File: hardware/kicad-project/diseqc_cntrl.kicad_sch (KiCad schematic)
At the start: 27 parts, among them IC1 TPS560200DBVR, J1 Barrel Jack

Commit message: Removed hand solder pads
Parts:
- C1, C2, C3, C4: footprint Capacitor_SMD:C_0603_1608Metric_Pad1.08x0.95mm_HandSolder -> Capacitor_SMD:C_0603_1608Metric
- FB2: footprint Inductor_SMD:L_0603_1608Metric_Pad1.05x0.95mm_HandSolder -> Inductor_SMD:L_0603_1608Metric
- R1, R2, R3, R4, R5: footprint Resistor_SMD:R_0603_1608Metric_Pad0.98x0.95mm_HandSolder -> Resistor_SMD:R_0603_1608Metric
- TP1, TP2, TP26, TP27, TP3, TP5: now left out of the parts list
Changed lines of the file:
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@@
 			)
 		)
-		(property "Footprint" "Resistor_SMD:R_0603_1608Metric_Pad0.98x0.95mm_HandSolder"
+		(property "Footprint" "Resistor_SMD:R_0603_1608Metric"
 			(at 94.742 116.84 90)
 			(hide yes)
@@
 			)
 		)
-		(property "Footprint" "Capacitor_SMD:C_0603_1608Metric_Pad1.08x0.95mm_HandSolder"
+		(property "Footprint" "Capacitor_SMD:C_0603_1608Metric"
 			(at 154.94 38.4048 0)
 			(hide yes)
@@
 			)
 		)
-		(property "Footprint" "Resistor_SMD:R_0603_1608Metric_Pad0.98x0.95mm_HandSolder"
+		(property "Footprint" "Resistor_SMD:R_0603_1608Metric"
 			(at 167.132 57.15 90)
 			(hide yes)
@@
 		(body_style 1)
 		(exclude_from_sim no)
-		(in_bom yes)
+		(in_bom no)
 		(on_board yes)
 		(in_pos_files yes)
@@
 		(body_style 1)
 		(exclude_from_sim no)
-		(in_bom yes)
+		(in_bom no)
 		(on_board yes)
 		(in_pos_files yes)
@@
 		(body_style 1)
 		(exclude_from_sim no)
-		(in_bom yes)
+		(in_bom no)
 		(on_board yes)
 		(in_pos_files yes)
@@
 		(body_style 1)
 		(exclude_from_sim no)
-		(in_bom yes)
+		(in_bom no)
 		(on_board yes)
 		(in_pos_files yes)
@@
 			)
 		)
-		(property "Footprint" "Resistor_SMD:R_0603_1608Metric_Pad0.98x0.95mm_HandSolder"
+		(property "Footprint" "Resistor_SMD:R_0603_1608Metric"
 			(at 167.132 46.99 90)
 			(hide yes)
@@
 			)
 		)
-		(property "Footprint" "Capacitor_SMD:C_0603_1608Metric_Pad1.08x0.95mm_HandSolder"
+		(property "Footprint" "Capacitor_SMD:C_0603_1608Metric"
 			(at 79.7052 120.65 0)
 			(hide yes)
@@
 		(body_style 1)
 		(exclude_from_sim no)
-		(in_bom yes)
+		(in_bom no)
 		(on_board yes)
 		(in_pos_files yes)
@@
 			)
 		)
-		(property "Footprint" "Resistor_SMD:R_0603_1608Metric_Pad0.98x0.95mm_HandSolder"
+		(property "Footprint" "Resistor_SMD:R_0603_1608Metric"
 			(at 94.742 129.54 90)
 			(hide yes)
@@
 			)
 		)
-		(property "Footprint" "Inductor_SMD:L_0603_1608Metric_Pad1.05x0.95mm_HandSolder"
+		(property "Footprint" "Inductor_SMD:L_0603_1608Metric"
 			(at 132.08 145.288 90)
 			(hide yes)
@@
 		(body_style 1)
 		(exclude_from_sim no)
-		(in_bom yes)
+		(in_bom no)
 		(on_board yes)
 		(in_pos_files yes)
@@
 			)
 		)
-		(property "Footprint" "Resistor_SMD:R_0603_1608Metric_Pad0.98x0.95mm_HandSolder"
+		(property "Footprint" "Resistor_SMD:R_0603_1608Metric"
 			(at 29.21 114.808 90)
 			(hide yes)
@@
 			)
 		)
-		(property "Footprint" "Capacitor_SMD:C_0603_1608Metric_Pad1.08x0.95mm_HandSolder"
+		(property "Footprint" "Capacitor_SMD:C_0603_1608Metric"
 			(at 105.1052 50.8 0)
 			(hide yes)
@@
 			)
 		)
-		(property "Footprint" "Capacitor_SMD:C_0603_1608Metric_Pad1.08x0.95mm_HandSolder"
+		(property "Footprint" "Capacitor_SMD:C_0603_1608Metric"
 			(at 87.3252 120.65 0)
 			(hide yes)

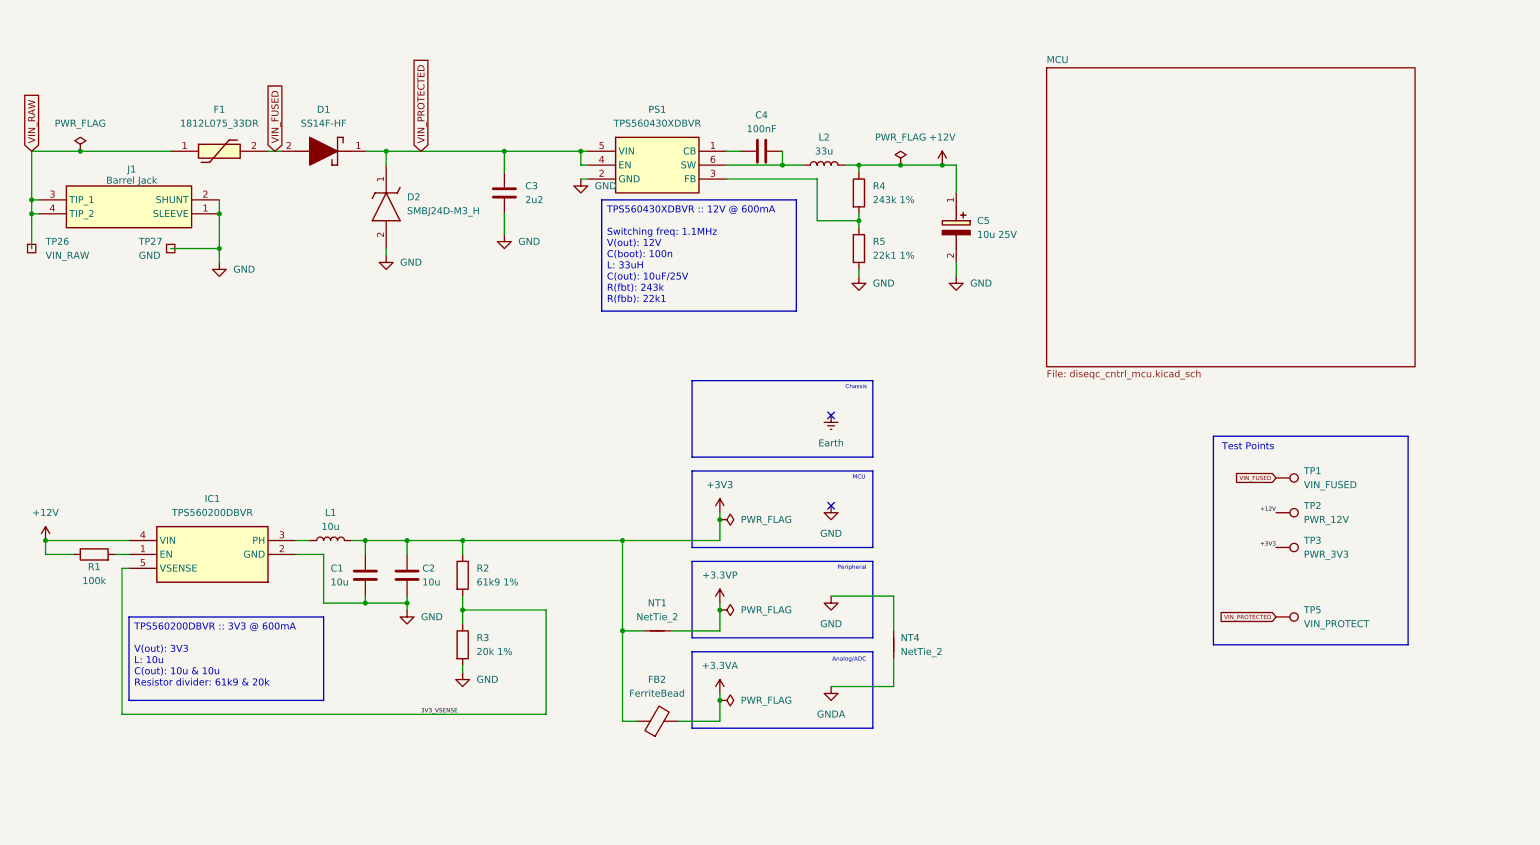
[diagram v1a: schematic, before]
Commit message: Update power supply ICs
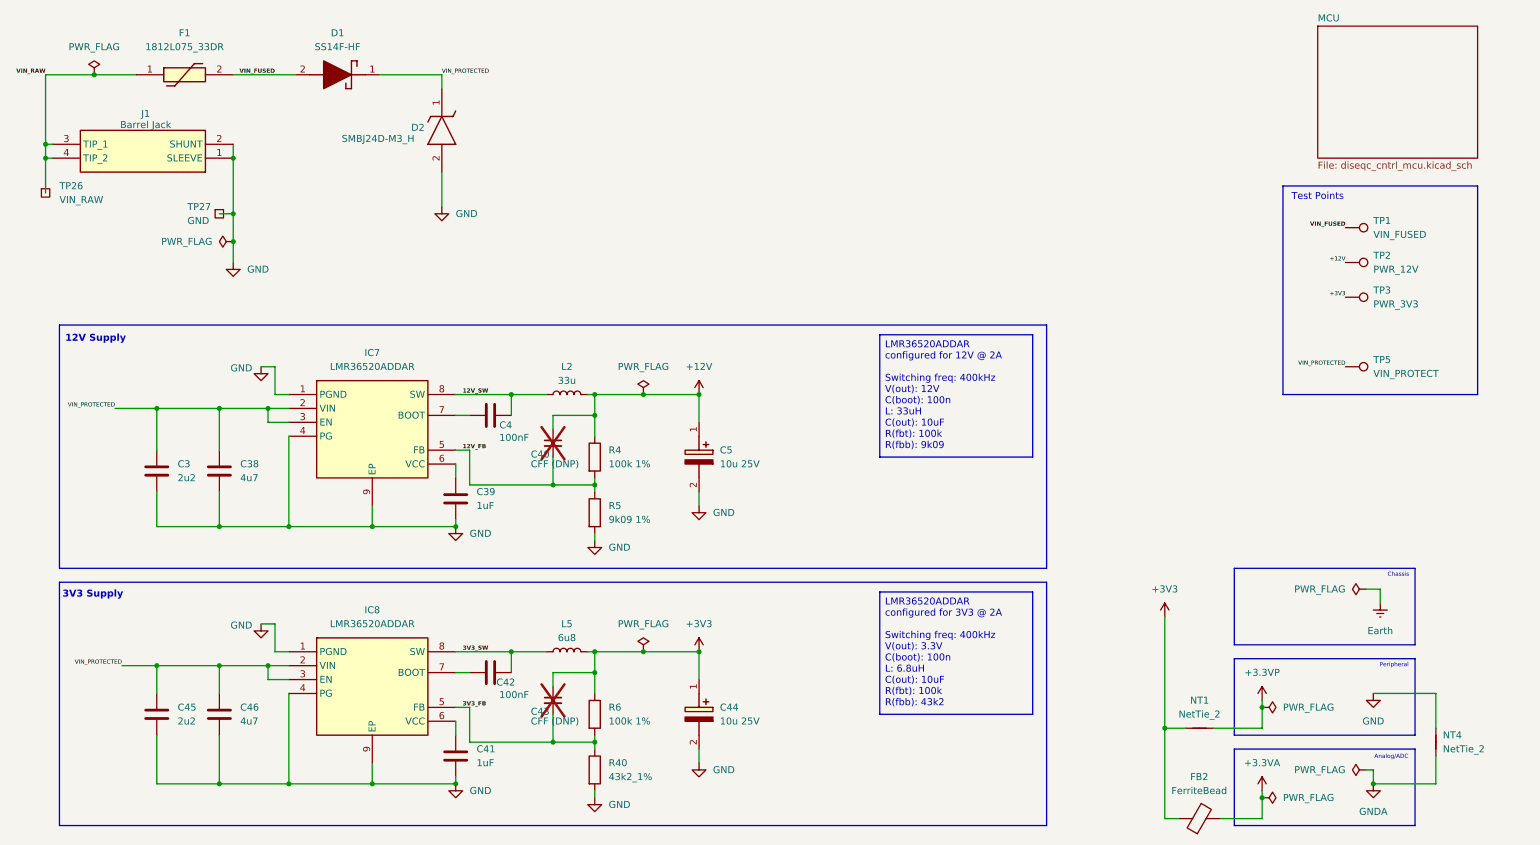
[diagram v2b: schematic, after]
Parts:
- removed C1: 10u, Capacitor_SMD:C_0603_1608Metric, symbol #InvenTree:C_10u_0603
- removed C2: 10u, Capacitor_SMD:C_0603_1608Metric, symbol diseqc_cntrl:C
- removed IC1: TPS560200DBVR, diseqc_cntrl:SOT95P280X145-5N, symbol diseqc_cntrl:TPS560200DBVR
- removed L1: 10u, Inductor_SMD:L_0603_1608Metric_Pad1.05x0.95mm_HandSolder, symbol diseqc_cntrl:L
- removed PS1: TPS560430XDBVR, diseqc_cntrl:SOT95P280X145-6N, symbol tps5604:TPS560430XDBVR
- removed R1: 100k, Resistor_SMD:R_0603_1608Metric, symbol diseqc_cntrl:R
- removed R2: 61k9 1%, Resistor_SMD:R_0603_1608Metric, symbol #InvenTree:R_61k9_0603_1%
- removed R3: 20k 1%, Resistor_SMD:R_0603_1608Metric, symbol #InvenTree:R_20k_0603_1%
- removed R4: 243k 1%, Resistor_SMD:R_0603_1608Metric, symbol diseqc_cntrl:R
- removed R5: 22k1 1%, Resistor_SMD:R_0603_1608Metric, symbol diseqc_cntrl:R
- added C38, C46: 4u7, Capacitor_SMD:C_0603_1608Metric, symbol #InvenTree:C_4u7_0603
- added C39, C41: 1uF, Capacitor_SMD:C_0603_1608Metric, symbol #InvenTree:C_1u_0603
- added C40, C43: CFF (DNP), symbol diseqc_cntrl:C_Small
- added C42: 100nF, Capacitor_SMD:C_0603_1608Metric, symbol diseqc_cntrl:C
- added C44: 10u 25V, diseqc_cntrl:CAPAE400X550N, symbol diseqc_cntrl:865080440002
- added C45: 2u2, Capacitor_SMD:C_0603_1608Metric, symbol diseqc_cntrl:C
- added IC7, IC8: LMR36520ADDAR, ebnx_footprints:SOIC127P600X170-9N, symbol ebnx_symbols:LMR36520ADDAR
- added L5: 6u8, Inductor_SMD:L_0805_2012Metric, symbol #InvenTree:L_6u8_0805
- added R4, R6: 100k 1%, Resistor_SMD:R_0603_1608Metric, symbol #InvenTree:R_100k_0603_1%
- added R40: 43k2_1%, Resistor_SMD:R_0603_1608Metric, symbol #InvenTree:R_43k2_0603_1%
- added R5: 9k09 1%, Resistor_SMD:R_0603_1608Metric, symbol #InvenTree:R_9k09_0603_1%
- L2: footprint diseqc_cntrl:INDPM3030X150N -> ebnx_footprints:INDPM3030X150N
- TP3: now in the parts list
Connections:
- net +12V: now also C40.1, R4.1
- net +3V3: now also C43.1, C44.1 (+), L5.2, R6.1
- net GND: now also C38.2, C39.2, C41.2, C44.2 (-), C45.2, C46.2, IC7.1 (PGND), IC7.4 (PG), IC7.9 (EP), IC8.1 (PGND), IC8.4 (PG), IC8.9 (EP), R40.2, R5.2
- net VIN_PROTECTED: now also C38.1, C45.1, C46.1, IC7.2 (VIN), IC7.3 (EN), IC8.2 (VIN), IC8.3 (EN)
- net at C4.1: now also IC7.7 (BOOT)
- net 12V_SW: now reaches C4.2, L2.1
- net 12V_SW: now also IC7.8 (SW)
- new net: C41.1, IC8.6 (VCC)
- new net: C39.1, IC7.6 (VCC)
- new net: C42.1, IC8.7 (BOOT)
- new net 12V_FB: C40.2, IC7.5 (FB), R4.2, R5.1
- new net 3V3_FB: C43.2, IC8.5 (FB), R40.1, R6.2
- new net 3V3_SW: C42.2, IC8.8 (SW), L5.1
- no-connect marks 2 -> 0
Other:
- note added: "12V Supply"
- note added: "3V3 Supply"
- note removed: "MCU"
- moved on the sheet: D1, D2, F1, FB2, J1, NT1, NT4, TP1, TP2, TP26, TP27, TP3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

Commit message: Renumbered/annotated
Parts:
- renumbered C3 to C1, C43 to C10, C5 to C11, C44 to C12, C45 to C2, C38 to C3, C46 to C4, C39 to C5, C41 to C6, C4 to C7, C42 to C8, C40 to C9, FB2 to FB1, IC7 to IC1, IC8 to IC2, L2 to L1, L5 to L2, NT4 to NT2, R4 to R1, R5 to R2, R6 to R3, R40 to R4, TP26 to TP1, TP27 to TP2, TP1 to TP3, TP2 to TP4, TP3 to TP5, TP5 to TP6

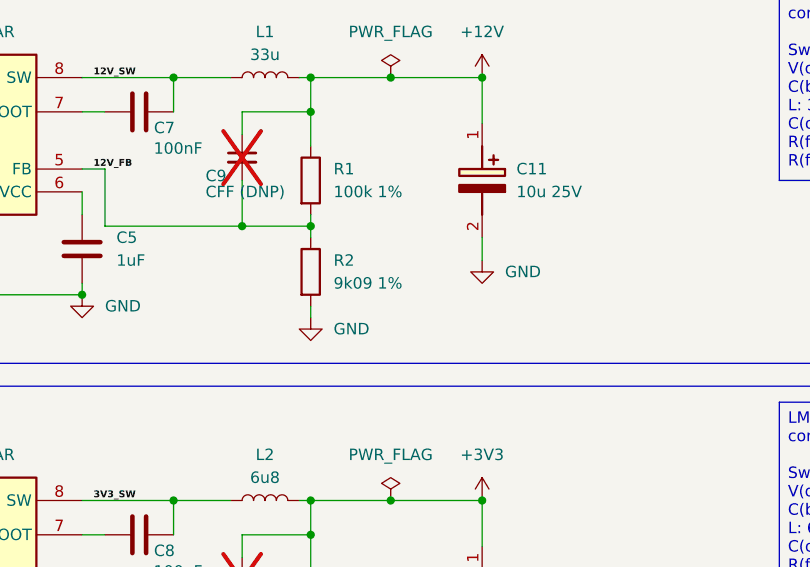
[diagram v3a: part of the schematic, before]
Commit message: Decreased VBUS_SENSE (R8) to 1k
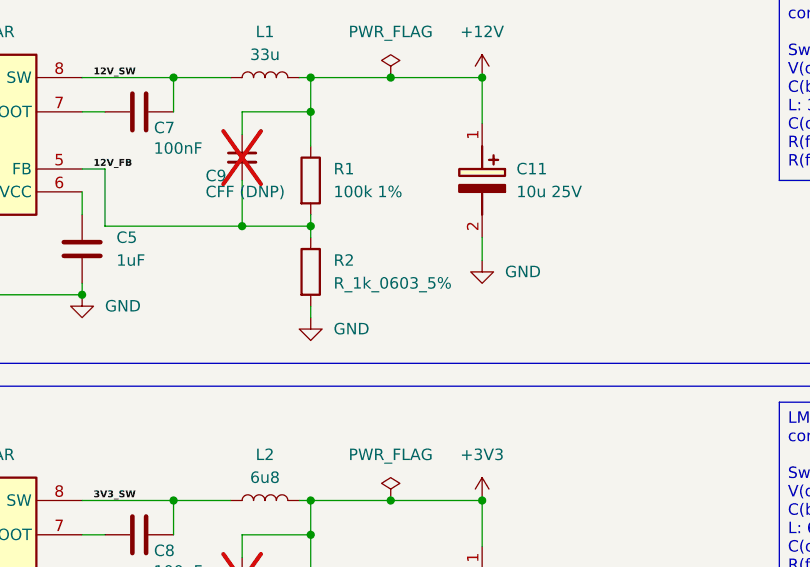
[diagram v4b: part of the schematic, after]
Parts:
- C11, C12: footprint diseqc_cntrl:CAPAE400X550N -> CAPAE400X550N
- IC1, IC2: InvenTree (none) -> 263; InvenTree Part (none) -> VREG_LMR36520
- R2: value 9k09 1% -> R_1k_0603_5%; footprint Resistor_SMD:R_0603_1608Metric -> Resistor_SMD:R_0603_1608Metric_Pad0.98x0.95mm_HandSolder; symbol #InvenTree:R_9k09_0603_1% -> #InvenTree:R_1k_0603_5%; InvenTree 265 -> 176; Part URL https://inventree.ebnx.net/web/part/265/ -> https://inventree.ebnx.net/web/part/176/; Tolerance (none) -> 5%
- TP5: now left out of the parts list
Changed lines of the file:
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@@
 			)
 		)
-		(property "Footprint" "diseqc_cntrl:CAPAE400X550N"
+		(property "Footprint" "CAPAE400X550N"
 			(at 43.51 144.78 0)
 			(hide yes)
@@
 	)
 	(symbol
-		(lib_name "TestPoint_Annotated_Silkscreen_1")
 		(lib_id "ebnx_symbols:TestPoint_Annotated_Silkscreen")
 		(at 257.81 66.04 270)
@@
 		(body_style 1)
 		(exclude_from_sim no)
-		(in_bom yes)
+		(in_bom no)
 		(on_board yes)
 		(in_pos_files yes)
@@
 	)
 	(symbol
-		(lib_name "C_1u_0603_1")
 		(lib_id "#InvenTree:C_1u_0603")
 		(at 95.25 102.87 0)
@@
 			)
 		)
-		(property "Footprint" "diseqc_cntrl:CAPAE400X550N"
+		(property "Footprint" "CAPAE400X550N"
 			(at 43.51 97.79 0)
 			(hide yes)
@@
 	)
 	(symbol
-		(lib_id "#InvenTree:R_9k09_0603_1%")
+		(lib_id "#InvenTree:R_1k_0603_5%")
 		(at 120.65 105.41 0)
 		(unit 1)
@@
 			)
 		)
-		(property "Value" "9k09 1%"
+		(property "Value" "R_1k_0603_5%"
 			(at 123.19 106.6799 0)
 			(show_name no)
@@
 			)
 		)
-		(property "Footprint" "Resistor_SMD:R_0603_1608Metric"
+		(property "Footprint" "Resistor_SMD:R_0603_1608Metric_Pad0.98x0.95mm_HandSolder"
 			(at 118.872 105.41 90)
 			(hide yes)
@@
 			)
 		)
-		(property "Tolerance" ""
+		(property "Tolerance" "5%"
 			(at 120.65 105.41 0)
 			(hide yes)
@@
 			)
 		)
-		(property "InvenTree" "265"
+		(property "InvenTree" "176"
 			(at 120.65 105.41 0)
 			(hide yes)
@@
 			)
 		)
-		(property "Part URL" "https://inventree.ebnx.net/web/part/265/"
+		(property "Part URL" "https://inventree.ebnx.net/web/part/176/"
 			(at 120.65 105.41 0)
 			(hide yes)
@@
 			)
 		)
+		(property "InvenTree" "263"
+			(at 64.77 83.82 0)
+			(hide yes)
+			(show_name no)
+			(do_not_autoplace no)
+			(effects
+				(font
+					(size 0.762 0.762)
+				)
+			)
+		)
+		(property "InvenTree Part" "VREG_LMR36520"
+			(at 64.77 83.82 0)
+			(hide yes)
+			(show_name no)
+			(do_not_autoplace no)
+			(effects
+				(font
+					(size 0.762 0.762)
+				)
+			)
+		)
 		(pin "3"
 		)
@@
 	)
 	(symbol
+		(lib_name "LMR36520ADDAR_1")
 		(lib_id "ebnx_symbols:LMR36520ADDAR")
 		(at 64.77 130.81 0)
@@
 			)
 		)
+		(property "InvenTree" "263"
+			(at 64.77 130.81 0)
+			(hide yes)
+			(show_name no)
+			(do_not_autoplace no)
+			(effects
+				(font
+					(size 0.762 0.762)
+				)
+			)
+		)
+		(property "InvenTree Part" "VREG_LMR36520"
+			(at 64.77 130.81 0)
+			(hide yes)
+			(show_name no)
+			(do_not_autoplace no)
+			(effects
+				(font
+					(size 0.762 0.762)
+				)
+			)
+		)
